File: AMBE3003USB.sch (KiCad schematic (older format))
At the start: 96 parts, among them J1 McBSP, J2 ACONF, J3 CODEC, J4 USB_OTG, P1 CONFIG, U1 AMBE3003, U2 LD1117S33TR, U3 TPS3805, U4 FT232RL, U5 TPS78319, X1 29.4912

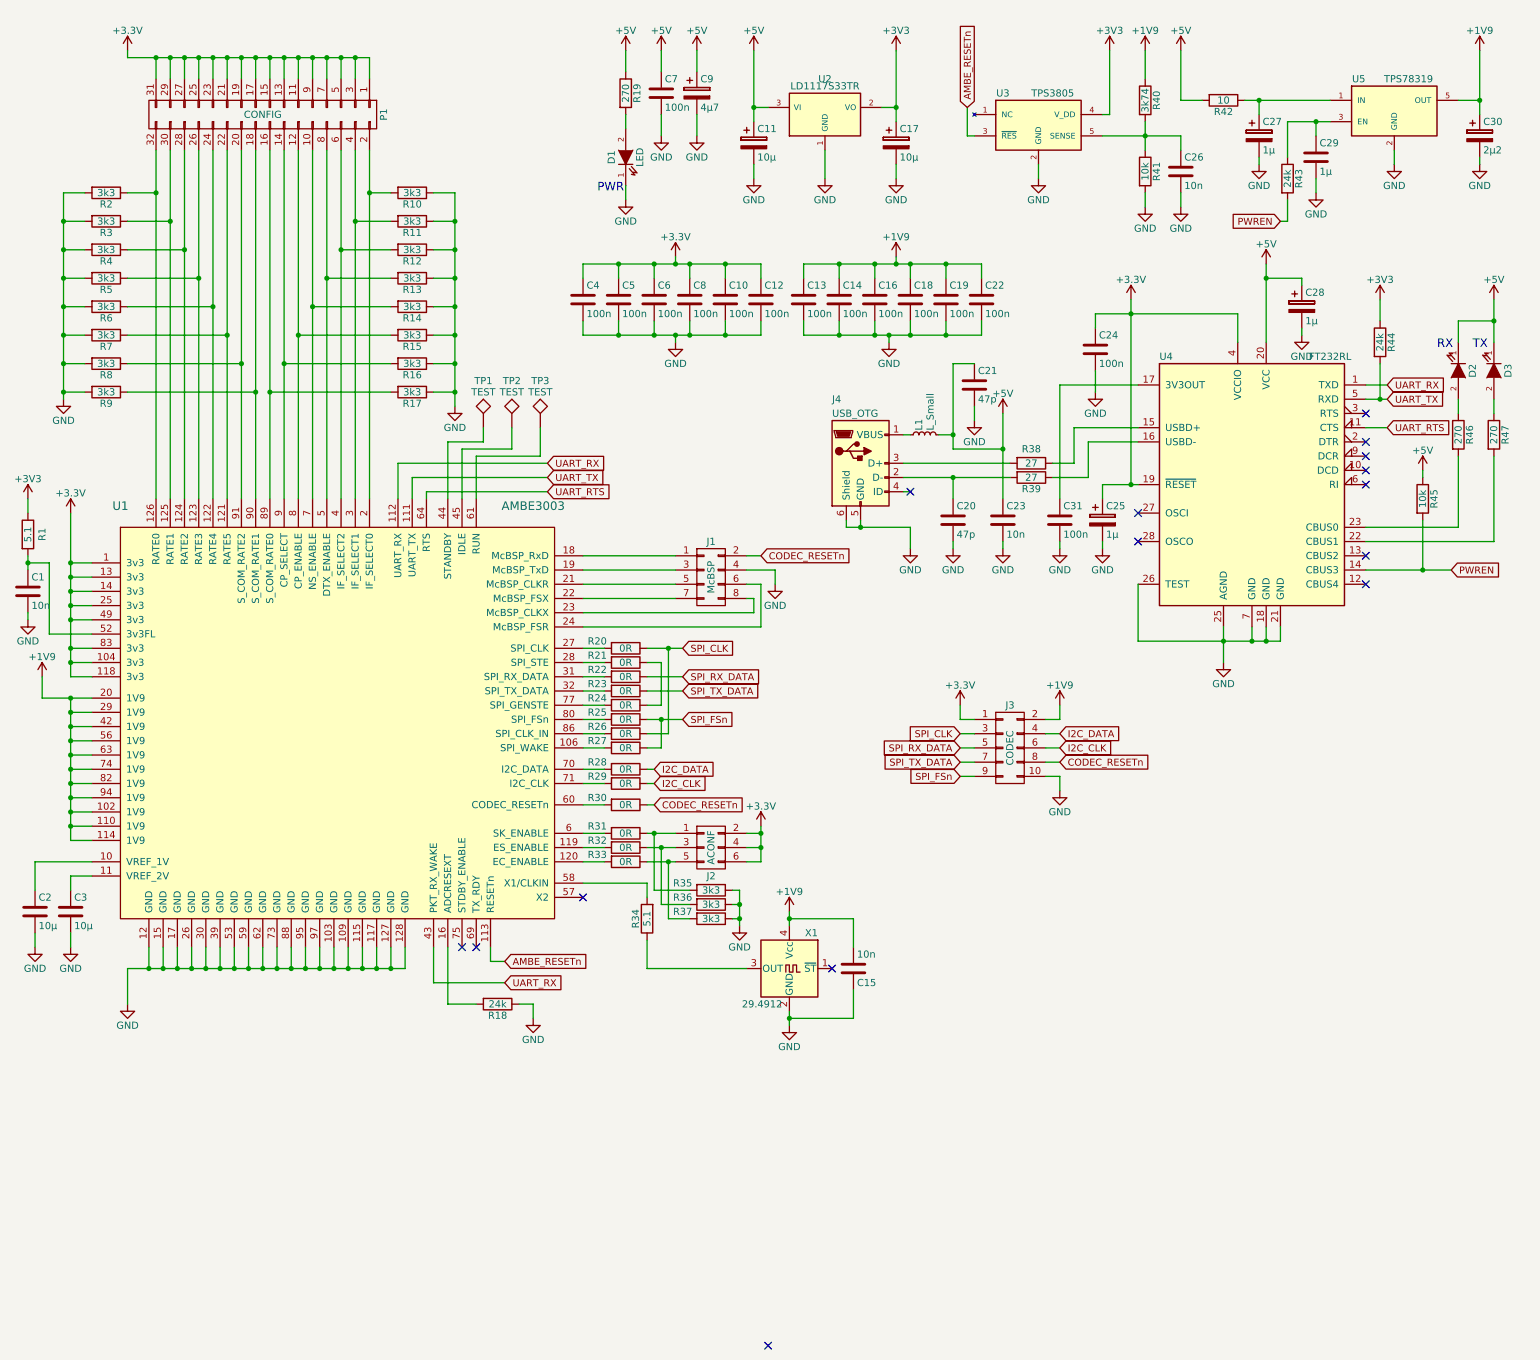
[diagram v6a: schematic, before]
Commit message: Added nice net names / labels
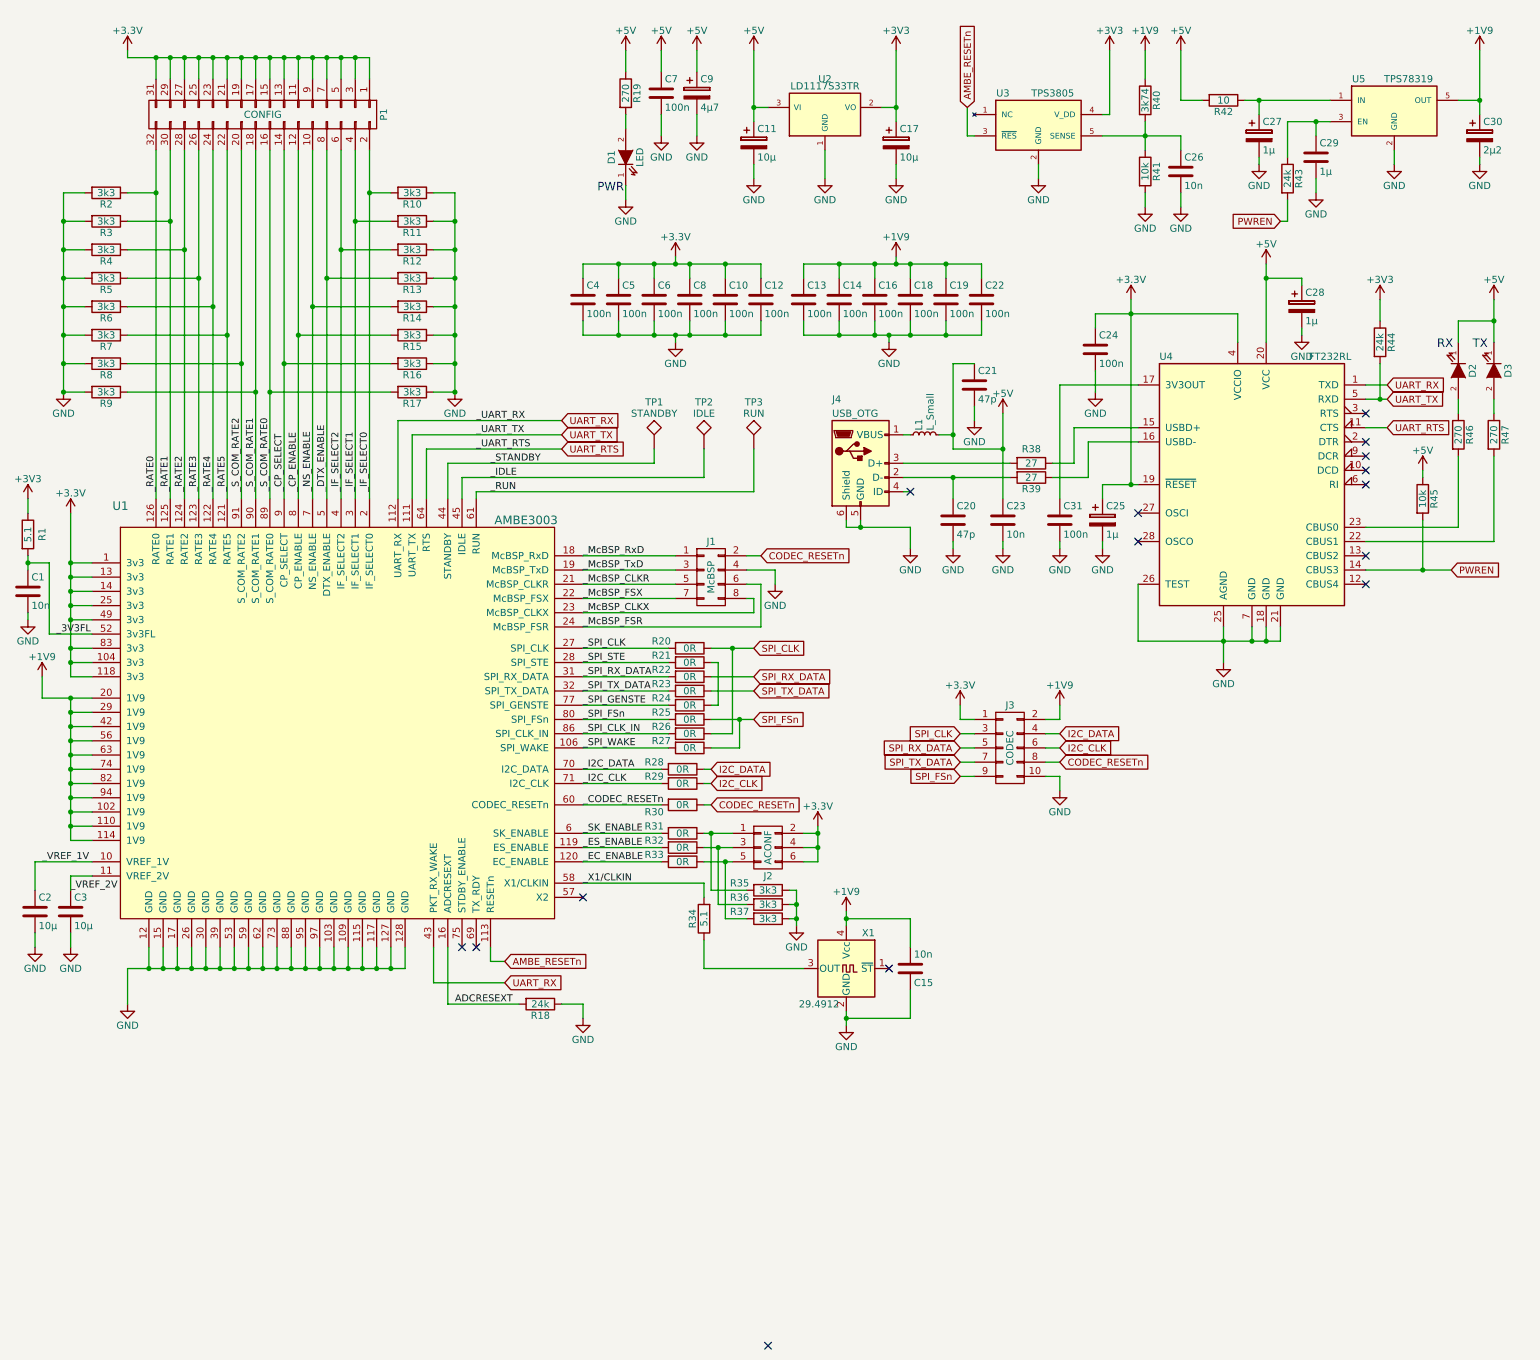
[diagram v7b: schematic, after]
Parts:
- TP1: value TEST -> STANDBY
- TP2: value TEST -> IDLE
- TP3: value TEST -> RUN
- U1: footprint Housings_QFP:LQFP-128_14x14mm_Pitch0.4mm -> (none)
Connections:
- net _IF_SELECT0: now reaches P1.2 (P2), R10.2, U1.2 (IF_SELECT0)
- net _IF_SELECT2: now reaches P1.6 (P6), R12.2, U1.4 (IF_SELECT2)
- net _IF_SELECT1: now reaches P1.4 (P4), R11.2, U1.3 (IF_SELECT1)
- net _NS_ENABLE: now reaches P1.10 (P10), R14.2, U1.7 (NS_ENABLE)
- net _CP_ENABLE: now reaches P1.12 (P12), R15.2, U1.8 (CP_ENABLE)
- net _CP_SELECT: now reaches P1.14 (P14), R16.2, U1.9 (CP_SELECT)
- net _S_COM_RATE0: now reaches P1.16 (P16), R17.2, U1.89 (S_COM_RATE0)
- net _S_COM_RATE1: now reaches P1.18 (P18), R9.1, U1.90 (S_COM_RATE1)
- net _S_COM_RATE2: now reaches P1.20 (P20), R8.1, U1.91 (S_COM_RATE2)
- net _RATE5: now reaches P1.22 (P22), R7.1, U1.121 (RATE5)
- net _RATE4: now reaches P1.24 (P24), R6.1, U1.122 (RATE4)
- net _RATE3: now reaches P1.26 (P26), R5.1, U1.123 (RATE3)
- net _RATE2: now reaches P1.28 (P28), R4.1, U1.124 (RATE2)
- net _RATE1: now reaches P1.30 (P30), R3.1, U1.125 (RATE1)
- net _RATE0: now reaches P1.32 (P32), R2.1, U1.126 (RATE0)
- net _DTX_ENABLE: now reaches P1.8 (P8), R13.2, U1.5 (DTX_ENABLE)
- net _X1/CLKIN: now reaches R34.2, U1.58 (X1/CLKIN)
- net _3V3FL: now reaches C1.1, R1.2, U1.52 (3v3FL)
- net ADCRESEXT: now reaches R18.2, U1.16 (ADCRESEXT)
- net _RUN: now reaches TP3.1, U1.61 (RUN)
- net _IDLE: now reaches TP2.1, U1.45 (IDLE)
- net _STANDBY: now reaches TP1.1, U1.44 (STANDBY)
- net _VREF_2V: now reaches C3.1, U1.11 (VREF_2V)
- net _VREF_1V: now reaches C2.1, U1.10 (VREF_1V)
- net _SPI_WAKE: now reaches R27.2, U1.106 (SPI_WAKE)
- net _ES_ENABLE: now reaches R32.2, U1.119 (ES_ENABLE)
- net _EC_ENABLE: now reaches R33.2, U1.120 (EC_ENABLE)
- net _McBSP_RxD: now reaches J1.1 (P1), U1.18 (McBSP_RxD)
- net _McBSP_TxD: now reaches J1.3 (P3), U1.19 (McBSP_TxD)
- net _McBSP_CLKR: now reaches J1.5 (P5), U1.21 (McBSP_CLKR)
- net _McBSP_FSX: now reaches J1.7 (P7), U1.22 (McBSP_FSX)
- net _McBSP_CLKX: now reaches J1.8 (P8), U1.23 (McBSP_CLKX)
- net _McBSP_FSR: now reaches J1.6 (P6), U1.24 (McBSP_FSR)
- net _SPI_CLK: now reaches R20.2, U1.27 (SPI_CLK)
- net _SPI_STE: now reaches R21.2, U1.28 (SPI_STE)
- net _SPI_RX_DATA: now reaches R22.2, U1.31 (SPI_RX_DATA)
- net _SPI_TX_DATA: now reaches R23.2, U1.32 (SPI_TX_DATA)
- net _SK_ENABLE: now reaches R31.2, U1.6 (SK_ENABLE)
- net _CODEC_RESETn: now reaches R30.2, U1.60 (CODEC_RESETn)
- net _I2C_DATA: now reaches R28.2, U1.70 (I2C_DATA)
- net _I2C_CLK: now reaches R29.2, U1.71 (I2C_CLK)
- net _SPI_GENSTE: now reaches R24.2, U1.77 (SPI_GENSTE)
- net _SPI_FSn: now reaches R25.2, U1.80 (SPI_FSn)
- net _SPI_CLK_IN: now reaches R26.2, U1.86 (SPI_CLK_IN)
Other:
- moved on the sheet: C15, J2, R18, R20, R21, R22, R23, R24, R25, R26, R27, R28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

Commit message: Add some more labels
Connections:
- net D+: now reaches J4.3 (D+), R38.2
- net D-: now reaches C20.1, J4.2 (D-), R39.2
- net VBUS: now reaches J4.1 (VBUS), L1.1
- net SK_ENABLE: now reaches J2.1 (P1), R31.1, R35.2
- net ES_ENABLE: now reaches J2.3 (P3), R32.1, R36.2
- net EC_ENABLE: now reaches J2.5 (P5), R33.1, R37.2
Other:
- moved on the sheet: J2, J4
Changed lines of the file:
@@
 L CONN_02X03 J2
 U 1 1 5928D899
-P 5900 6300
-F 0 "J2" H 5900 6100 50  0000 C CNN
-F 1 "ACONF" V 5900 6300 50  0000 C CNN
-F 2 "Pin_Headers:Pin_Header_Straight_2x03_Pitch2.54mm" H 5900 5100 50  0001 C CNN
-F 3 "" H 5900 5100 50  0001 C CNN
-	1    5900 6300
+P 6450 6300
+F 0 "J2" H 6450 6100 50  0000 C CNN
+F 1 "ACONF" V 6450 6300 50  0000 C CNN
+F 2 "Pin_Headers:Pin_Header_Straight_2x03_Pitch2.54mm" H 6450 5100 50  0001 C CNN
+F 3 "" H 6450 5100 50  0001 C CNN
+	1    6450 6300
 	1    0    0    -1
 $EndComp
@@
 L +3.3V #PWR047
 U 1 1 5928F66B
-P 6250 6150
-F 0 "#PWR047" H 6250 6000 50  0001 C CNN
-F 1 "+3.3V" H 6250 6290 50  0000 C CNN
-F 2 "" H 6250 6150 50  0000 C CNN
-F 3 "" H 6250 6150 50  0000 C CNN
-	1    6250 6150
+P 6950 6150
+F 0 "#PWR047" H 6950 6000 50  0001 C CNN
+F 1 "+3.3V" H 6950 6290 50  0000 C CNN
+F 2 "" H 6950 6150 50  0000 C CNN
+F 3 "" H 6950 6150 50  0000 C CNN
+	1    6950 6150
 	1    0    0    -1
 $EndComp
@@
 L USB_OTG-RESCUE-AMBE3003USB J4
 U 1 1 592902DE
-P 6550 3600
-F 0 "J4" H 6350 4050 50  0000 L CNN
-F 1 "USB_OTG" H 6350 3950 50  0000 L CNN
-F 2 "Connectors:USB_Mini-B" H 6700 3550 50  0001 C CNN
-F 3 "" H 6700 3550 50  0001 C CNN
-	1    6550 3600
+P 6300 3600
+F 0 "J4" H 6100 4050 50  0000 L CNN
+F 1 "USB_OTG" H 6100 3950 50  0000 L CNN
+F 2 "Connectors:USB_Mini-B" H 6450 3550 50  0001 C CNN
+F 3 "" H 6450 3550 50  0001 C CNN
+	1    6300 3600
 	1    0    0    -1
 $EndComp
@@
 	1    0    0    -1
 $EndComp
-NoConn ~ 6900 3800
+NoConn ~ 6600 3800
 NoConn ~ 4600 6650
 $Comp
@@
 Text Label 4600 6200 0    49   ~ 0
 _SK_ENABLE
-Text Label 4600 6300 0    49   ~ 0
-_ES_ENABLE
 Text Label 4600 6400 0    49   ~ 0
 _EC_ENABLE
@@
 	5450 6550 5450 6650
 Wire Wire Line
-	5450 6200 5650 6200
-Wire Wire Line
-	5450 6300 5650 6300
-Wire Wire Line
-	5450 6400 5650 6400
+	5450 6200 6200 6200
+Wire Wire Line
+	5450 6300 6200 6300
 Wire Wire Line
 	8250 4150 8250 4200
@@
 	7100 3400 7200 3400
 Wire Wire Line
-	6850 3400 6900 3400
-Connection ~ 6550 4050
-Wire Wire Line
-	6550 4050 6550 4000
-Wire Wire Line
-	6450 4050 6450 4000
-Wire Wire Line
-	6900 4200 6900 4050
+	6600 3400 6900 3400
+Wire Wire Line
+	6900 4050 6900 4200
 Wire Wire Line
 	7250 5800 7350 5800
@@
 Wire Wire Line
 	6100 6800 6050 6800
-Connection ~ 5600 6400
 Wire Wire Line
 	5600 6800 5750 6800
 Wire Wire Line
-	5600 6400 5600 6800
-Connection ~ 5550 6300
-Wire Wire Line
 	5550 6700 5750 6700
-Wire Wire Line
-	5550 6300 5550 6700
 Connection ~ 5500 6200
 Wire Wire Line
@@
 Wire Wire Line
 	5500 6200 5500 6600
-Connection ~ 6250 6300
-Wire Wire Line
-	6250 6400 6150 6400
-Connection ~ 6250 6200
-Wire Wire Line
-	6250 6300 6150 6300
-Wire Wire Line
-	6250 6150 6250 6400
-Wire Wire Line
-	6150 6200 6250 6200
 Wire Wire Line
 	4600 6400 5150 6400
@@
 Connection ~ 6650 2700
 Wire Wire Line
-	6650 2600 6650 2700
+	6650 2700 6650 2600
 Connection ~ 6900 2700
 Wire Wire Line
-	6900 2600 6900 2700
+	6900 2700 6900 2600
 Connection ~ 7150 2700
 Wire Wire Line
-	7150 2600 7150 2700
+	7150 2700 7150 2600
 Connection ~ 6750 2700
 Wire Wire Line
@@
 Connection ~ 6650 2200
 Wire Wire Line
-	6650 2300 6650 2200
+	6650 2200 6650 2300
 Connection ~ 6900 2200
 Wire Wire Line
-	6900 2300 6900 2200
+	6900 2200 6900 2300
 Connection ~ 7150 2200
 Wire Wire Line
-	7150 2300 7150 2200
+	7150 2200 7150 2300
 Connection ~ 6800 2200
 Wire Wire Line
@@
 	7550 3250 7550 3850
 Connection ~ 7550 3500
-Wire Wire Line
-	6850 3800 6900 3800
 Wire Wire Line
 	10750 2750 10750 2600
@@
 	8050 3600 7900 3600
 Wire Wire Line
-	6850 3600 7600 3600
-Wire Wire Line
-	6850 3700 7600 3700
+	6600 3600 7600 3600
+Wire Wire Line
+	6600 3700 7600 3700
 Wire Wire Line
 	7900 3700 8150 3700
@@
 	7550 4200 7550 4150
 Wire Wire Line
-	6900 4050 6450 4050
+	6200 4050 6900 4050
 Wire Wire Line
 	7200 3700 7200 3850
@@
 Text Label 4600 6550 0    49   ~ 0
 _X1/CLKIN
+Text Label 6650 3600 0    49   ~ 0
+D+
+Text Label 6650 3700 0    49   ~ 0
+D-
+Text Label 6650 3400 0    49   ~ 0
+VBUS
+Wire Wire Line
+	6200 4050 6200 4000
+Wire Wire Line
+	6300 4000 6300 4050
+Connection ~ 6300 4050
+Text Label 4600 6300 0    49   ~ 0
+_ES_ENABLE
+Text Label 5700 6200 0    49   ~ 0
+SK_ENABLE
+Text Label 5700 6300 0    49   ~ 0
+ES_ENABLE
+Wire Wire Line
+	5450 6400 6200 6400
+Wire Wire Line
+	5550 6700 5550 6300
+Connection ~ 5550 6300
+Wire Wire Line
+	5600 6800 5600 6400
+Connection ~ 5600 6400
+Wire Wire Line
+	6700 6200 6950 6200
+Wire Wire Line
+	6950 6150 6950 6400
+Wire Wire Line
+	6950 6300 6700 6300
+Connection ~ 6950 6200
+Wire Wire Line
+	6950 6400 6700 6400
+Connection ~ 6950 6300
+Text Label 5700 6400 0    49   ~ 0
+EC_ENABLE
 $EndSCHEMATC
